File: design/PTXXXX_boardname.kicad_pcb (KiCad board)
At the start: 4 copper layers, 150 x 100 mm, 4 parts

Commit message: added simple PCB stackup drawing on F.Fab layer added dimensions on Dwgs.User as example, updated fab text to match
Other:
- board text added: "B.Cu - Bottom Copper"
- board text added: "F.Cu - Front Copper"
- board text added: "INSTRUCTIONS: =========== MULTILAYER, SURFACE MOUNT & THROUGH HOLE 4 (2 SIGNAL & POUR, 2 SPLIT PLANE) MIN 0.2MM TRACK / 0.20MM GAP / 0.30MM DRILL 90Z DIFF PAIR, OUTER (0.25MM TRACK / 0.15MM GAP / 0.12MM TO INNER) FR4 OR EQUIVALENT, PCB RATED UL94V-0 35um OUTERS AND 17.5um INNERS ENIG GREEN WHITE 100.0MM X 150.0MM 1.6MM +/- 10% MAX OVER PLATING NOT REQUIRED NOT REQUIRED NOT REQUIRED SEEK APPROVAL 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"
- board text added: "In1.Cu - Inner Layer 1 Copper"
- board text added: "In2.Cu - Inner Layer 2 Copper"
- board text added: "PCB STACKUP =========="
- board text removed: "INSTRUCTIONS: =========== MULTILAYER, SURFACE MOUNT & THROUGH HOLE 4 (2 SIGNAL & POUR, 2 SPLIT PLANE) MIN 0.2MM TRACK / 0.20MM GAP / 0.30MM DRILL 90Z DIFF PAIR, OUTER (0.25MM TRACK / 0.15MM GAP / 0.12MM TO INNER) FR4 OR EQUIVALENT, PCB RATED UL94V-0 35um OUTERS AND 17.5um INNERS ENIG GREEN WHITE ??.0MM X ??.0MM 1.6MM +/- 10% MAX OVER PLATING NOT REQUIRED NOT REQUIRED NOT REQUIRED SEEK APPROVAL YE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"
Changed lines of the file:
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@@
   (general
     (thickness 1.6)
-    (drawings 35)
+    (drawings 53)
     (tracks 0)
     (zones 0)
@@
       (net 1 GND))
   )
+  (dimension 20 (width 0.12) (layer F.Fab)
+    (gr_text "1.60mm +/- 10%" (at 211.760001 64.5 90) (layer F.Fab)
+      (effects (font (size 1 1) (thickness 0.12)))
+    )
+    (feature1 (pts (xy 224.5 74.5) (xy 212.41358 74.5)))
+    (feature2 (pts (xy 224.5 54.5) (xy 212.41358 54.5)))
+    (crossbar (pts (xy 213.000001 54.5) (xy 213.000001 74.5)))
+    (arrow1a (pts (xy 213.000001 74.5) (xy 212.41358 73.373496)))
+    (arrow1b (pts (xy 213.000001 74.5) (xy 213.586422 73.373496)))
+    (arrow2a (pts (xy 213.000001 54.5) (xy 212.41358 55.626504)))
+    (arrow2b (pts (xy 213.000001 54.5) (xy 213.586422 55.626504)))
+  )
+  (gr_line (start 226 54.5) (end 226 74.5) (layer F.Fab) (width 0.05))
+  (gr_line (start 241 54.5) (end 241 74.5) (layer F.Fab) (width 0.05))
+  (dimension 2.5 (width 0.12) (layer F.Fab)
+    (gr_text 0.12mm (at 217.5 55.5 90) (layer F.Fab)
+      (effects (font (size 1 1) (thickness 0.12)) (justify right))
+    )
+    (feature1 (pts (xy 224.5 55) (xy 218.913579 55)))
+    (feature2 (pts (xy 224.5 57.5) (xy 218.913579 57.5)))
+    (crossbar (pts (xy 219.5 57.5) (xy 219.5 55)))
+    (arrow1a (pts (xy 219.5 55) (xy 220.086421 56.126504)))
+    (arrow1b (pts (xy 219.5 55) (xy 218.913579 56.126504)))
+    (arrow2a (pts (xy 219.5 57.5) (xy 220.086421 56.373496)))
+    (arrow2b (pts (xy 219.5 57.5) (xy 218.913579 56.373496)))
+  )
+  (dimension 2.5 (width 0.12) (layer F.Fab)
+    (gr_text 0.12mm (at 217.5 73.5 90) (layer F.Fab)
+      (effects (font (size 1 1) (thickness 0.12)) (justify left))
+    )
+    (feature1 (pts (xy 224.5 71.5) (xy 218.913579 71.5)))
+    (feature2 (pts (xy 224.5 74) (xy 218.913579 74)))
+    (crossbar (pts (xy 219.5 74) (xy 219.5 71.5)))
+    (arrow1a (pts (xy 219.5 71.5) (xy 220.086421 72.626504)))
+    (arrow1b (pts (xy 219.5 71.5) (xy 218.913579 72.626504)))
+    (arrow2a (pts (xy 219.5 74) (xy 220.086421 72.873496)))
+    (arrow2b (pts (xy 219.5 74) (xy 218.913579 72.873496)))
+  )
+  (gr_text "In2.Cu - Inner Layer 2 Copper" (at 242.5 71) (layer F.Fab)
+    (effects (font (size 1 1) (thickness 0.15)) (justify left))
+  )
+  (gr_text "In1.Cu - Inner Layer 1 Copper" (at 242.5 58) (layer F.Fab)
+    (effects (font (size 1 1) (thickness 0.15)) (justify left))
+  )
+  (gr_text "B.Cu - Bottom Copper" (at 242.5 74.5) (layer F.Fab)
+    (effects (font (size 1 1) (thickness 0.15)) (justify left))
+  )
+  (gr_text "F.Cu - Front Copper" (at 242.5 54.5) (layer F.Fab)
+    (effects (font (size 1 1) (thickness 0.15)) (justify left))
+  )
+  (gr_poly (pts (xy 241 74.5) (xy 226 74.5) (xy 226 74) (xy 241 74)) (layer F.Fab) (width 0.1))
+  (gr_poly (pts (xy 241 71.5) (xy 226 71.5) (xy 226 71) (xy 241 71)) (layer F.Fab) (width 0.1))
+  (gr_poly (pts (xy 241 58) (xy 226 58) (xy 226 57.5) (xy 241 57.5)) (layer F.Fab) (width 0.1))
+  (gr_text "PCB STACKUP\n==========" (at 233.5 47) (layer F.Fab)
+    (effects (font (size 1.2 1.2) (thickness 0.2)))
+  )
+  (gr_poly (pts (xy 241 55) (xy 226 55) (xy 226 54.5) (xy 241 54.5)) (layer F.Fab) (width 0.1))
+  (dimension 100 (width 0.12) (layer Dwgs.User)
+    (gr_text "100.000 mm" (at 25.56 110 270) (layer Dwgs.User)
+      (effects (font (size 1 1) (thickness 0.12)))
+    )
+    (feature1 (pts (xy 40 160) (xy 26.213579 160)))
+    (feature2 (pts (xy 40 60) (xy 26.213579 60)))
+    (crossbar (pts (xy 26.8 60) (xy 26.8 160)))
+    (arrow1a (pts (xy 26.8 160) (xy 26.213579 158.873496)))
+    (arrow1b (pts (xy 26.8 160) (xy 27.386421 158.873496)))
+    (arrow2a (pts (xy 26.8 60) (xy 26.213579 61.126504)))
+    (arrow2b (pts (xy 26.8 60) (xy 27.386421 61.126504)))
+  )
+  (dimension 88 (width 0.12) (layer Dwgs.User)
+    (gr_text "88.000 mm" (at 32.86 110 90) (layer Dwgs.User)
+      (effects (font (size 1 1) (thickness 0.12)))
+    )
+    (feature1 (pts (xy 46 66) (xy 33.513579 66)))
+    (feature2 (pts (xy 46 154) (xy 33.513579 154)))
+    (crossbar (pts (xy 34.1 154) (xy 34.1 66)))
+    (arrow1a (pts (xy 34.1 66) (xy 34.686421 67.126504)))
+    (arrow1b (pts (xy 34.1 66) (xy 33.513579 67.126504)))
+    (arrow2a (pts (xy 34.1 154) (xy 34.686421 152.873496)))
+    (arrow2b (pts (xy 34.1 154) (xy 33.513579 152.873496)))
+  )
+  (dimension 138 (width 0.12) (layer Dwgs.User)
+    (gr_text "138.000 mm" (at 115 51.96) (layer Dwgs.User)
+      (effects (font (size 1 1) (thickness 0.12)))
+    )
+    (feature1 (pts (xy 184 66) (xy 184 52.613579)))
+    (feature2 (pts (xy 46 66) (xy 46 52.613579)))
+    (crossbar (pts (xy 46 53.2) (xy 184 53.2)))
+    (arrow1a (pts (xy 184 53.2) (xy 182.873496 53.786421)))
+    (arrow1b (pts (xy 184 53.2) (xy 182.873496 52.613579)))
+    (arrow2a (pts (xy 46 53.2) (xy 47.126504 53.786421)))
+    (arrow2b (pts (xy 46 53.2) (xy 47.126504 52.613579)))
+  )
+  (dimension 150 (width 0.12) (layer Dwgs.User)
+    (gr_text "150.000 mm" (at 115 45.86) (layer Dwgs.User)
+      (effects (font (size 1 1) (thickness 0.12)))
+    )
+    (feature1 (pts (xy 190 60) (xy 190 46.513579)))
+    (feature2 (pts (xy 40 60) (xy 40 46.513579)))
+    (crossbar (pts (xy 40 47.1) (xy 190 47.1)))
+    (arrow1a (pts (xy 190 47.1) (xy 188.873496 47.686421)))
+    (arrow1b (pts (xy 190 47.1) (xy 188.873496 46.513579)))
+    (arrow2a (pts (xy 40 47.1) (xy 41.126504 47.686421)))
+    (arrow2b (pts (xy 40 47.1) (xy 41.126504 46.513579)))
+  )
   (target plus (at 40 160) (size 5) (width 0.05) (layer Edge.Cuts))
   (gr_text "FABRICATION\n===========\nSUMMARY:\nLAYER COUNT:\nDESIGN RULES:\nIMPEDANCE CONTROL:\n\nMATERIAL:\nCOPPER WEIGHT:\nFINISH:\nRESIST COLOUR:\nSILKSCREEN COLOUR:\nDIMENSIONS:\nFINISHED THICKNESS:\nEDGE PLATING:\nEDGE CONNECTORS:\nEDGE CHAMFERING:\nTHIEVING/VENTING:\nROHS/LEAD FREE:\nDRILLING:\nPLUGGING:\nOTHER NOTES:" (at 225.2 114.9) (layer F.Fab)
     (effects (font (size 1.2 1.2) (thickness 0.2)) (justify right))
   )
-  (gr_text "INSTRUCTIONS:\n===========\nMULTILAYER, SURFACE MOUNT & THROUGH HOLE\n4 (2 SIGNAL & POUR, 2 SPLIT PLANE)\nMIN 0.2MM TRACK / 0.20MM GAP / 0.30MM DRILL\n90Z DIFF PAIR, OUTER\n    (0.25MM TRACK / 0.15MM GAP / 0.12MM TO INNER)\nFR4 OR EQUIVALENT, PCB RATED UL94V-0\n35um OUTERS AND 17.5um INNERS\nENIG\nGREEN\nWHITE\n??.0MM X ??.0MM\n1.6MM +/- 10% MAX OVER PLATING\nNOT REQUIRED\nNOT REQUIRED\nNOT REQUIRED\nSEEK APPROVAL\nYES\nSEE DRILL FILE. HOLE SIZES ARE FINISHED.\nNOT REQUIRED\nNONE" (at 226.2 114.9) (layer F.Fab)
+  (gr_text "INSTRUCTIONS:\n===========\nMULTILAYER, SURFACE MOUNT & THROUGH HOLE\n4 (2 SIGNAL & POUR, 2 SPLIT PLANE)\nMIN 0.2MM TRACK / 0.20MM GAP / 0.30MM DRILL\n90Z DIFF PAIR, OUTER\n    (0.25MM TRACK / 0.15MM GAP / 0.12MM TO INNER)\nFR4 OR EQUIVALENT, PCB RATED UL94V-0\n35um OUTERS AND 17.5um INNERS\nENIG\nGREEN\nWHITE\n100.0MM X 150.0MM\n1.6MM +/- 10% MAX OVER PLATING\nNOT REQUIRED\nNOT REQUIRED\nNOT REQUIRED\nSEEK APPROVAL\nYES\nSEE DRILL FILE. HOLE SIZES ARE FINISHED.\nNOT REQUIRED\nNONE" (at 226.2 114.9) (layer F.Fab)
     (effects (font (size 1.2 1.2) (thickness 0.2)) (justify left))
   )

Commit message: added Signal/GND/PWR names on layer stackup F.Fab drawing
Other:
- board text added: "B.Cu - Bottom Copper (Signal & GND)"
- board text added: "F.Cu - Front Copper (Signal & GND)"
- board text added: "In1.Cu - Inner Layer 1 Copper (GND)"
- board text added: "In2.Cu - Inner Layer 2 Copper (PWR)"
- board text removed: "B.Cu - Bottom Copper"
- board text removed: "F.Cu - Front Copper"
- board text removed: "In1.Cu - Inner Layer 1 Copper"
- board text removed: "In2.Cu - Inner Layer 2 Copper"
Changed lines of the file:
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@@
     (arrow2b (pts (xy 219.5 74) (xy 218.913579 72.873496)))
   )
-  (gr_text "In2.Cu - Inner Layer 2 Copper" (at 242.5 71) (layer F.Fab)
+  (gr_text "In2.Cu - Inner Layer 2 Copper (PWR)" (at 242.5 71) (layer F.Fab)
     (effects (font (size 1 1) (thickness 0.15)) (justify left))
   )
-  (gr_text "In1.Cu - Inner Layer 1 Copper" (at 242.5 58) (layer F.Fab)
+  (gr_text "In1.Cu - Inner Layer 1 Copper (GND)" (at 242.5 58) (layer F.Fab)
     (effects (font (size 1 1) (thickness 0.15)) (justify left))
   )
-  (gr_text "B.Cu - Bottom Copper" (at 242.5 74.5) (layer F.Fab)
+  (gr_text "B.Cu - Bottom Copper (Signal & GND)" (at 242.5 74.5) (layer F.Fab)
     (effects (font (size 1 1) (thickness 0.15)) (justify left))
   )
-  (gr_text "F.Cu - Front Copper" (at 242.5 54.5) (layer F.Fab)
+  (gr_text "F.Cu - Front Copper (Signal & GND)" (at 242.5 54.5) (layer F.Fab)
     (effects (font (size 1 1) (thickness 0.15)) (justify left))
   )

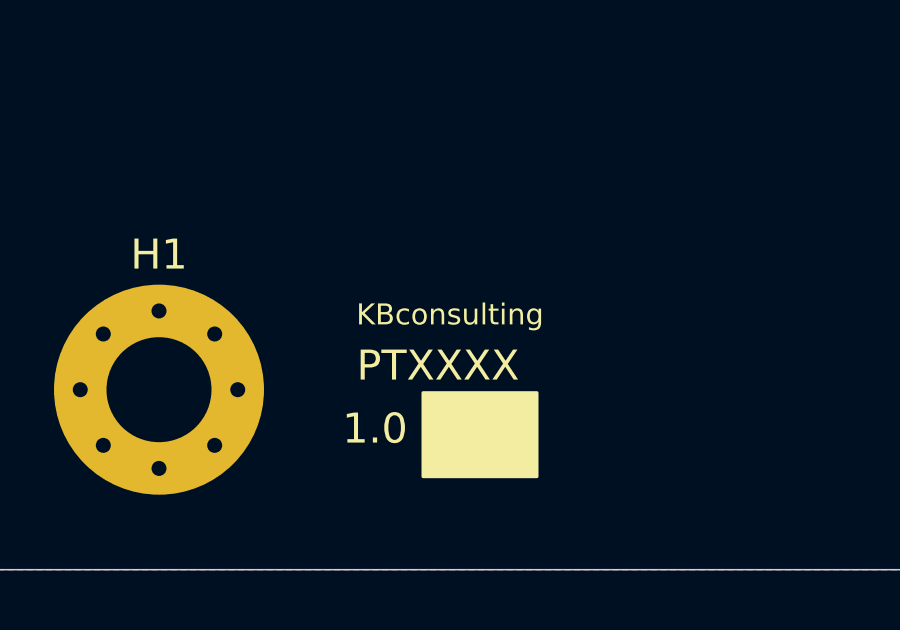
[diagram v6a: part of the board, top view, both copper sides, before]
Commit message: modified template KiCAD project to use new OptimisedPD titleblock changed PCB silkscreen text from KBconsulting to OptimisedPD updated library ref to use new OptimisedPD titleblock
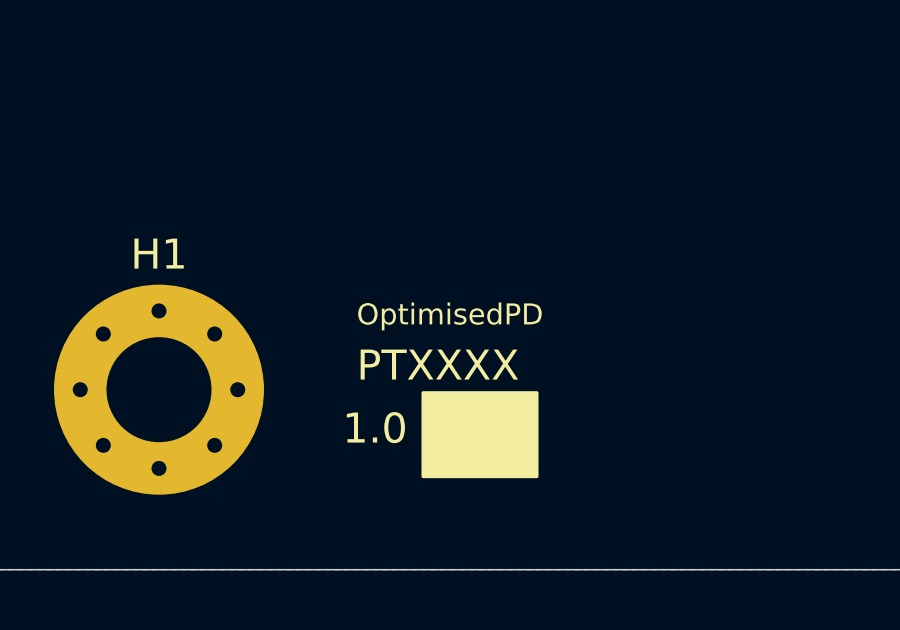
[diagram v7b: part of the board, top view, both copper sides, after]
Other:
- board text added: "OptimisedPD"
- board text removed: "KBconsulting"
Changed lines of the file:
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@@
     (effects (font (size 1.2 1.2) (thickness 0.2)) (justify left))
   )
-  (gr_text KBconsulting (at 55.7 151.5) (layer F.SilkS)
+  (gr_text OptimisedPD (at 55.7 151.5) (layer F.SilkS)
     (effects (font (size 0.7 0.7) (thickness 0.12)))
   )

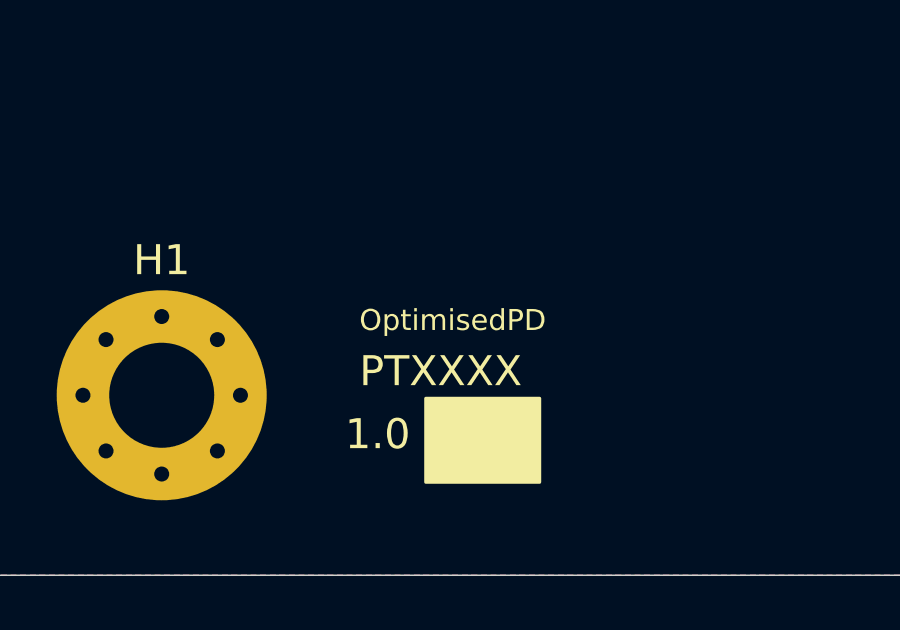
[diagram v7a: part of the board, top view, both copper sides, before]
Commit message: added LOGO1 for optimised silkscreen logo corrected titleblock reference, was still kbconsulting re-imported to PCB and placed optimised logo deleted silkscreen optimised text
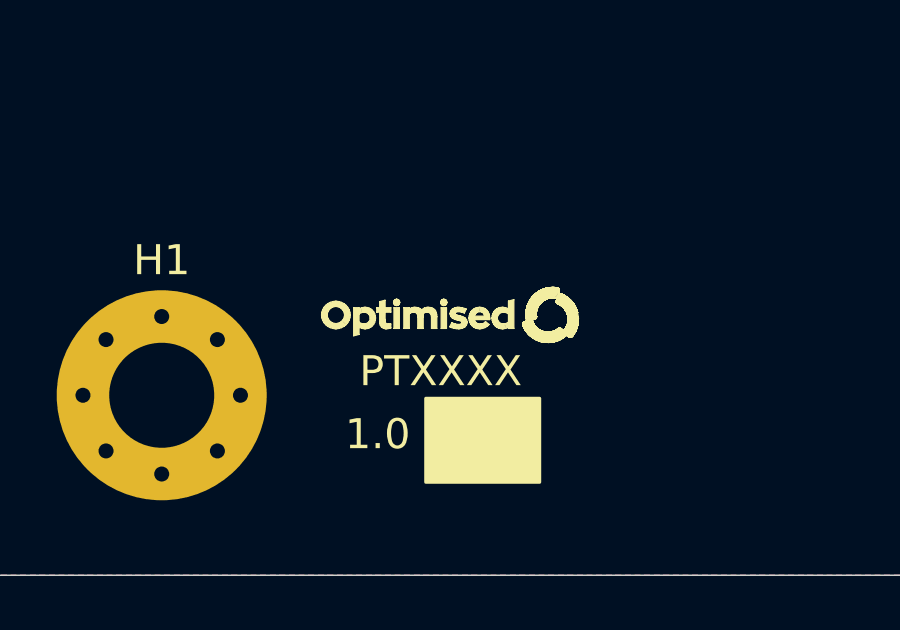
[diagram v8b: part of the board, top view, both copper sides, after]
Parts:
- added LOGO1: Optimised Logo, _kb_miscellaneous:PCB_Silk_Logo_Optimised, F.Cu at (55.5, 151.4)
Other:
- board text removed: "OptimisedPD"
